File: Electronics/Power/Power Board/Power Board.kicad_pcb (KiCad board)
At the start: 2 copper layers, 70 parts, among them IC1 STM32U575VGT6, IC2 TJA1057GT/3, IC3 INA219AIDR, IC4 INA219AIDR, IC6 TPS54295PWPR, IC7 MP28167GQ-A-Z, J1 XT60PW-M, J2 USB4056-03-A, J3 XT60PW-F, J4 Screw_Terminal_01x02, J5 TC2030

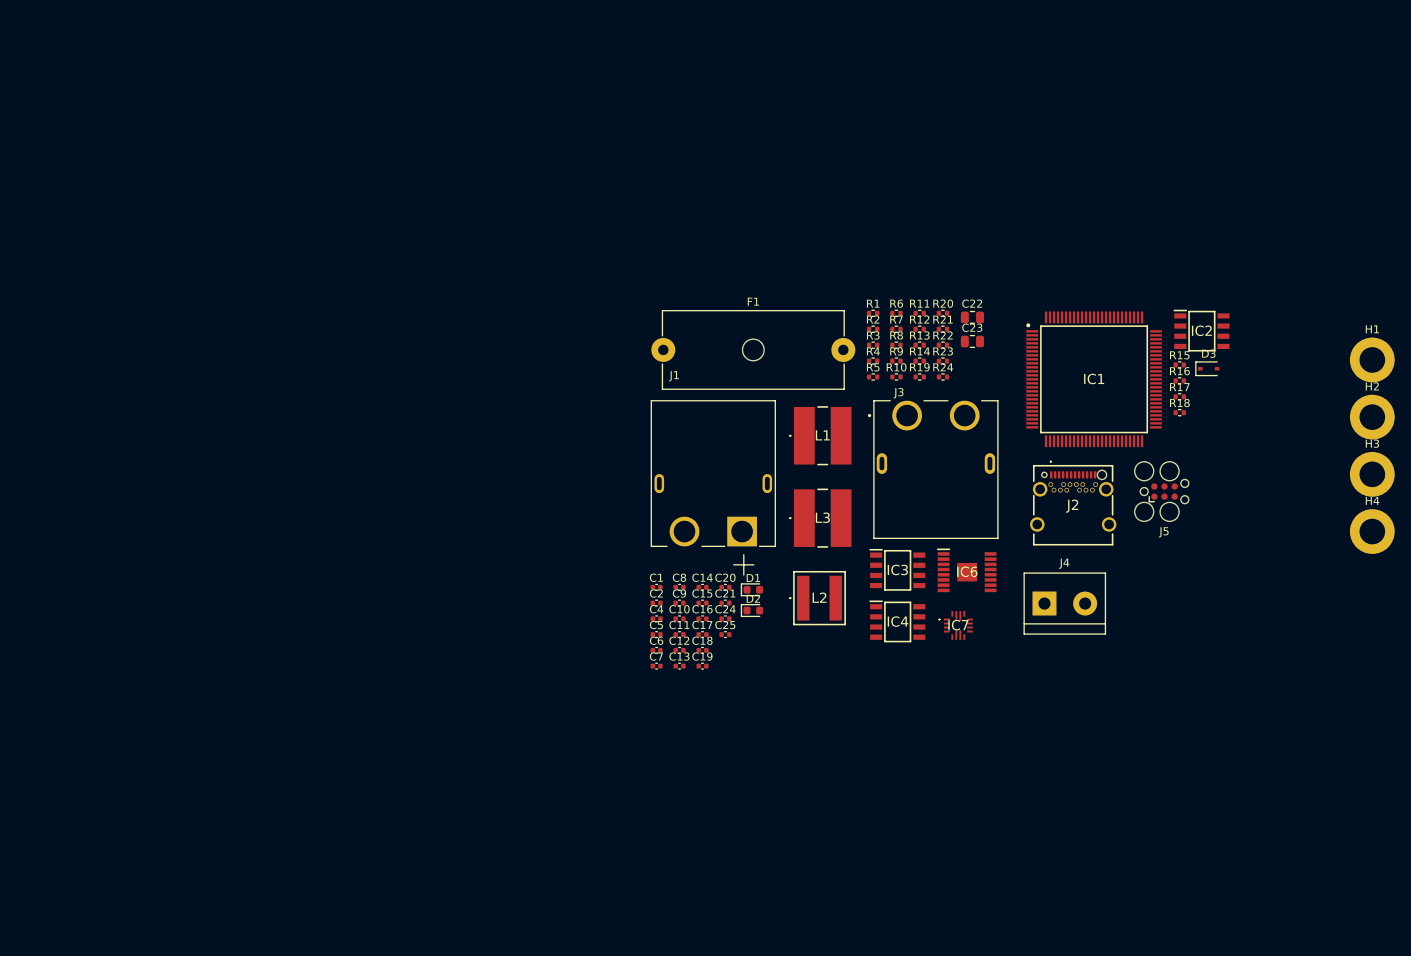
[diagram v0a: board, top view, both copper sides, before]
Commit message: Motor driver + power board progress
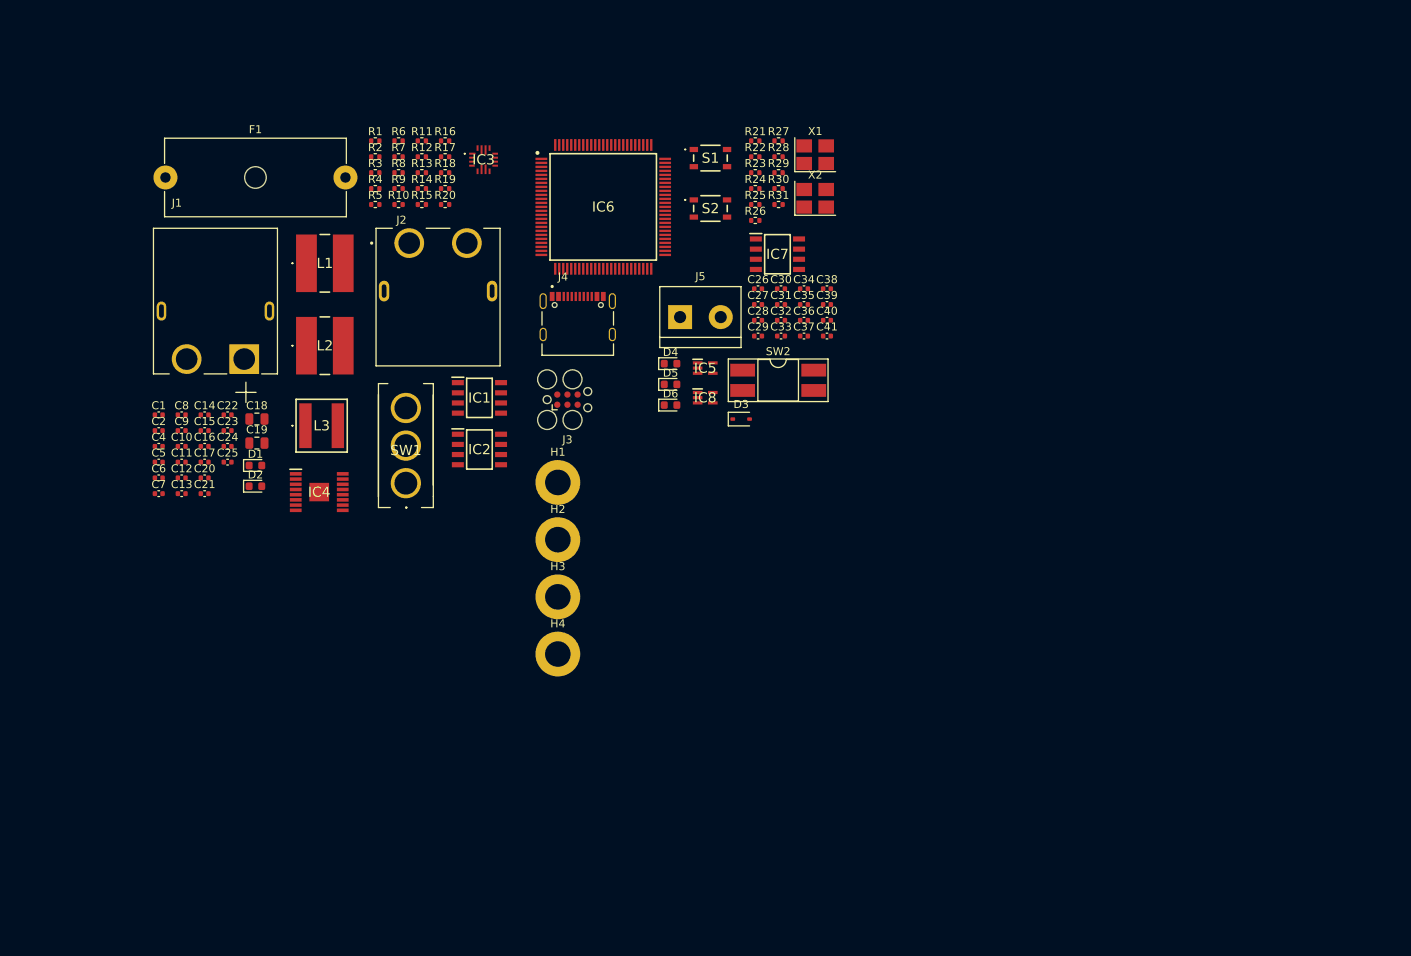
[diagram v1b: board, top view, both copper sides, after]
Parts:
- added C26: 10n, Capacitor_SMD:C_0402_1005Metric, F.Cu at (195.0, 72.2)
- added C27: 100n, Capacitor_SMD:C_0402_1005Metric, F.Cu at (195.0, 74.1)
- added C28: 100n, Capacitor_SMD:C_0402_1005Metric, F.Cu at (195.0, 76.1)
- added C29: 100n, Capacitor_SMD:C_0402_1005Metric, F.Cu at (195.0, 78.1)
- added C30: 100n, Capacitor_SMD:C_0402_1005Metric, F.Cu at (197.9, 72.2)
- added C31: 100n, Capacitor_SMD:C_0402_1005Metric, F.Cu at (197.9, 74.1)
- added C32: 100n, Capacitor_SMD:C_0402_1005Metric, F.Cu at (197.9, 76.1)
- added C33: 100n, Capacitor_SMD:C_0402_1005Metric, F.Cu at (197.9, 78.1)
- added C34: 100n, Capacitor_SMD:C_0402_1005Metric, F.Cu at (200.8, 72.2)
- added C35: 10u, Capacitor_SMD:C_0402_1005Metric, F.Cu at (200.8, 74.1)
- added C36: 4u7, Capacitor_SMD:C_0402_1005Metric, F.Cu at (200.8, 76.1)
- added C37: 100n, Capacitor_SMD:C_0402_1005Metric, F.Cu at (200.8, 78.1)
- added C38: 1u, Capacitor_SMD:C_0402_1005Metric, F.Cu at (203.6, 72.2)
- added C39: 100n, Capacitor_SMD:C_0402_1005Metric, F.Cu at (203.6, 74.1)
- added C40: 1u, Capacitor_SMD:C_0402_1005Metric, F.Cu at (203.6, 76.1)
- added C41: 10n, Capacitor_SMD:C_0402_1005Metric, F.Cu at (203.6, 78.1)
- added D4: Red, LED_SMD:LED_0603_1608Metric, F.Cu at (184.1, 81.5)
- added D5: Green, LED_SMD:LED_0603_1608Metric, F.Cu at (184.1, 84.1)
- added D6: Blue, LED_SMD:LED_0603_1608Metric, F.Cu at (184.1, 86.7)
- added IC5: ESDA6V1W5, footprints:SOT65P210X110-5N, F.Cu at (188.4, 82.1)
- added IC8: ESDA6V1W5, footprints:SOT65P210X110-5N, F.Cu at (188.4, 85.8)
- added R25: 5k1, Resistor_SMD:R_0402_1005Metric, F.Cu at (194.7, 61.6)
- added R26: 2k2, Resistor_SMD:R_0402_1005Metric, F.Cu at (194.7, 63.6)
- added R27: 10k, Resistor_SMD:R_0402_1005Metric, F.Cu at (197.6, 53.7)
- added R28: 10k, Resistor_SMD:R_0402_1005Metric, F.Cu at (197.6, 55.7)
- added R29: 1k5, Resistor_SMD:R_0402_1005Metric, F.Cu at (197.6, 57.6)
- added R30: 1k5, Resistor_SMD:R_0402_1005Metric, F.Cu at (197.6, 59.6)
- added R31: 1k5, Resistor_SMD:R_0402_1005Metric, F.Cu at (197.6, 61.6)
- added S1: TS20-42-25-WT-160-SMT-TR, MSL Footprints:TS204225WT160SMTTRMSL, F.Cu at (189.1, 55.8)
- added S2: TS20-42-25-WT-160-SMT-TR, MSL Footprints:TS204225WT160SMTTRMSL, F.Cu at (189.1, 62.1)
- added SW1: SW_SPDT, MSL Footprints:Toggle_switch, F.Cu at (151.0, 96.5)
- added SW2: SW_DIP_x02, Package_DIP:DIP-4_W8.89mm_SMDSocket_LongPads, F.Cu at (197.5, 83.6)
- added X1: 25MHz_Clock, Oscillator:Oscillator_SMD_Abracon_ASE-4Pin_3.2x2.5mm_HandSoldering, F.Cu at (202.2, 55.4)
- added X2: 32.768kHz_Clock, Oscillator:Oscillator_SMD_Abracon_ASE-4Pin_3.2x2.5mm_HandSoldering, F.Cu at (202.2, 60.8)
- C1, C17: value 10n -> 100n
- C10, C12: value 22u -> 10n
- C11: value 22u -> 1u
- C13, C14: value 22u -> 100n
- C15: value 10u -> 1u
- C16: value 10u -> 100n
- C18: value 10n -> 47u; footprint Capacitor_SMD:C_0402_1005Metric -> Capacitor_SMD:C_0805_2012Metric
- C19: value 100n -> 47u; footprint Capacitor_SMD:C_0402_1005Metric -> Capacitor_SMD:C_0805_2012Metric
- C2: value 1u -> 100n
- C21: value 1u -> 22u
- C22, C23: value 47u -> 22u; footprint Capacitor_SMD:C_0805_2012Metric -> Capacitor_SMD:C_0402_1005Metric
- C24, C25: value 100n -> 22u
- C6, C7: value 100n -> 10u
- C9: value 100n -> 10n
- IC1: value STM32U575VGT6 -> INA219AIDR; footprint MSL Footprints:QFP50P1600X1600X160-100N -> MSL Footprints:SOIC127P600X175-8N
- IC2: value TJA1057GT/3 -> INA219AIDR
- IC3: value INA219AIDR -> MP28167GQ-A-Z; footprint MSL Footprints:SOIC127P600X175-8N -> MSL Footprints:MP28167GQAZ
- IC4: value INA219AIDR -> TPS54295PWPR; footprint MSL Footprints:SOIC127P600X175-8N -> MSL Footprints:SOP65P640X120-17N
- IC6: value TPS54295PWPR -> STM32U575VGT6; footprint MSL Footprints:SOP65P640X120-17N -> MSL Footprints:QFP50P1600X1600X160-100N
- IC7: value MP28167GQ-A-Z -> TJA1057GT/3; footprint MSL Footprints:MP28167GQAZ -> MSL Footprints:SOIC127P600X175-8N
- J2: value USB4056-03-A -> XT60PW-F; footprint MSL Footprints:USB405603A -> MSL Footprints:AMASS_XT60PW-F
- J3: value XT60PW-F -> TC2030; footprint MSL Footprints:AMASS_XT60PW-F -> Connector:Tag-Connect_TC2030-IDC-FP_2x03_P1.27mm_Vertical
- J4: value Screw_Terminal_01x02 -> TYPE-C-31-M-12; footprint TerminalBlock:TerminalBlock_bornier-2_P5.08mm -> MSL Footprints:HRO_TYPE-C-31-M-12
- J5: value TC2030 -> Screw_Terminal_01x02; footprint Connector:Tag-Connect_TC2030-IDC-FP_2x03_P1.27mm_Vertical -> TerminalBlock:TerminalBlock_bornier-2_P5.08mm
- L2: value MPL-AL6050-4R7 -> 2u2; footprint MSL Footprints:MPLAL60504R7 -> MSL Footprints:29222C
- L3: value 2u2 -> MPL-AL6050-4R7; footprint MSL Footprints:29222C -> MSL Footprints:MPLAL60504R7
- R1: value 100k -> 22R
- R10: value 22k1 -> 787k
- R11: value 33k -> 0R
- R12: value 10k -> 0R
- R13: value 2k2 -> 430k
- R14: value 1k5 -> 39k2
- R15: value 5k1 -> 124k
- R16: value 5k1 -> 22k1
- R17: value 2k2 -> 33k
- R18: value 2k2 -> 10k
- R19, R23: value 10m -> 2k2
- R2: value 10k -> 10m
- R20: value 22R -> 1k5
- R21: value 22R -> 120R
- R22: value 22R -> 10k
- R24: value 22R -> 5k1
- R3, R4: value 0R -> 22R
- R5: value 430k -> 10m
- R6: value 787k -> 22R
- R7: value 39k2 -> 10k
- R8: value 21k5 -> 100k
- R9: value 124k -> 21k5
- moved H1 103.0 mm to (170.0, 96.4)
- moved H2 103.0 mm to (170.0, 103.5)
- moved H3 103.0 mm to (170.0, 110.7)
- moved H4 103.0 mm to (170.0, 117.8)
- moved R15 96.8 mm to (153.0, 61.6)
- moved R16 96.6 mm to (155.9, 53.7)
- moved R17 96.6 mm to (155.9, 55.7)
- moved R18 96.6 mm to (155.9, 57.6)
- moved C22 93.9 mm to (128.7, 87.9)
- moved C23 93.8 mm to (128.7, 89.9)
- moved IC2 91.5 mm to (160.2, 92.2)
- moved J2 85.9 mm to (155.0, 66.4)
- moved IC1 76.9 mm to (160.2, 85.8)
- moved IC4 74.1 mm to (140.2, 97.6)
- moved IC3 72.9 mm to (160.7, 56.0)
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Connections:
- C1 pad 1: GND -> /Power/12V_VIN+
- C1 pad 2: /Power/12V_EN -> /Power/12V_VIN-
- C10 pad 1: +12V -> GND
- C10 pad 2: GND -> /Power/12V_EN
- C11 pad 1: +12V -> GND
- C11 pad 2: GND -> /Power/3V65
- C12 pad 1: +12V -> /Power/OC
- C13 pad 1: +12V -> /Power/VBST1
- C13 pad 2: GND -> /Power/SW1
- C14 pad 1: +12V -> /Power/VBST2
- C14 pad 2: GND -> /Power/SW2
- C15 pad 1: VBAT -> /Power/VREG5
- C16 pad 1: VBAT -> /Power/12V_SW1
- C16 pad 2: GND -> /Power/BST12
- C17 pad 1: GND -> /Power/BST22
- C17 pad 2: /Power/SS1 -> /Power/12V_SW2
- C18 pad 1: GND -> +5V
- C18 pad 2: /Power/SS2 -> GND
- C19 pad 1: /Power/VBST1 -> +3V3
- C19 pad 2: /Power/SW1 -> GND
- C2 pad 1: GND -> /Power/BAT_VIN+
- C2 pad 2: /Power/3V65 -> /Power/BAT_VIN-
- C20 pad 1: /Power/VBST2 -> +12V
- C20 pad 2: /Power/SW2 -> GND
- C21 pad 1: /Power/VREG5 -> +12V
- C22 pad 1: +5V -> +12V
- C23 pad 1: +3V3 -> +12V
- C24 pad 1: /Power/12V_VIN+ -> +12V
- C24 pad 2: /Power/12V_VIN- -> GND
- C25 pad 1: /Power/BAT_VIN+ -> +12V
- C25 pad 2: /Power/BAT_VIN- -> GND
- C6 pad 1: /Power/12V_SW1 -> VBAT
- C6 pad 2: /Power/BST12 -> GND
- C7 pad 1: /Power/BST22 -> VBAT
- C7 pad 2: /Power/12V_SW2 -> GND
- C8 pad 1: /Power/OC -> GND
- C8 pad 2: GND -> /Power/SS1
- C9 pad 1: +12V -> GND
- C9 pad 2: GND -> /Power/SS2
- IC1 pad 1: unconnected-(IC1-PE2-Pad1) -> GND
- IC1 pad 2: unconnected-(IC1-PE3-Pad2) -> GND
- IC1 pad 3: unconnected-(IC1-PE4-Pad3) -> SDA
- IC1 pad 4: unconnected-(IC1-PE5-Pad4) -> SCL
- IC1 pad 5: unconnected-(IC1-PE6-Pad5) -> +3V3
- IC1 pad 6: unconnected-(IC1-VBAT-Pad6) -> GND
- IC1 pad 7: unconnected-(IC1-PC13-Pad7) -> /Power/12V_VIN-
- IC1 pad 8: OSC32_IN -> /Power/12V_VIN+
- IC2 pad 1: CAN_TX -> GND
- IC2 pad 2: GND -> +3V3
- IC2 pad 3: +5V -> SDA
- IC2 pad 4: CAN_RX -> SCL
- IC2 pad 6: /Control/CANL -> GND
- IC2 pad 7: /Control/CANH -> /Power/BAT_VIN-
- IC2 pad 8: SILENT -> /Power/BAT_VIN+
- IC3 pad 1: GND -> VBAT
- IC3 pad 3: SDA -> /Power/12V_EN
- IC3 pad 4: SCL -> ALT
- IC3 pad 5: +3V3 -> SCL
- IC3 pad 6: GND -> SDA
- IC3 pad 7: /Power/12V_VIN- -> /Power/OC
- IC3 pad 8: /Power/12V_VIN+ -> /Power/12V_FB
- IC4 pad 1: GND -> VBAT
- IC4 pad 2: +3V3 -> /Power/VBST1
- IC4 pad 3: SDA -> /Power/SW1
- IC4 pad 4: SCL -> GND
- IC4 pad 5: +3V3 -> VBAT
- IC4 pad 6: GND -> /Power/SS1
- IC4 pad 7: /Power/BAT_VIN- -> /Power/VFB1
- IC4 pad 8: /Power/BAT_VIN+ -> GND
- IC6 pad 1: VBAT -> unconnected-(IC6-PE2-Pad1)
- IC6 pad 10: /Power/VFB2 -> GND
- IC6 pad 11: /Power/SS2 -> +3V3
- IC6 pad 12: VBAT -> OSC25M
- IC6 pad 13: GND -> unconnected-(IC6-PH1-OSC_OUT-Pad13)
- IC6 pad 14: /Power/SW2 -> NRST
- IC6 pad 15: /Power/VBST2 -> unconnected-(IC6-PC0-Pad15)
- IC6 pad 16: VBAT -> unconnected-(IC6-PC1-Pad16)
- IC6 pad 17: GND -> unconnected-(IC6-PC2-Pad17)
- IC6 pad 2: /Power/VBST1 -> unconnected-(IC6-PE3-Pad2)
- IC6 pad 3: /Power/SW1 -> unconnected-(IC6-PE4-Pad3)
- IC6 pad 4: GND -> unconnected-(IC6-PE5-Pad4)
- IC6 pad 5: VBAT -> unconnected-(IC6-PE6-Pad5)
- IC6 pad 6: /Power/SS1 -> +3V3
- IC6 pad 7: /Power/VFB1 -> unconnected-(IC6-PC13-Pad7)
- IC6 pad 8: GND -> OSC32K
- IC6 pad 9: /Power/VREG5 -> unconnected-(IC6-PC15-OSC32_OUT-Pad9)
- IC7 pad 1: VBAT -> CAN_TX
- IC7 pad 3: /Power/12V_EN -> +5V
- IC7 pad 4: ALT -> CAN_RX
- IC7 pad 5: SCL -> +3V3
- IC7 pad 6: SDA -> /Control/CANL
- IC7 pad 7: /Power/OC -> /Control/CANH
- IC7 pad 8: /Power/12V_FB -> SILENT
- J3 pad 1: GND -> +3V3
- J3 pad 2: /Power/12V_OUT -> SWDIO
- J5 pad 1: +3V3 -> /Control/CANH
- J5 pad 2: SWDIO -> /Control/CANL
- L2 pad 1: /Power/12V_SW1 -> /Power/SW2
- L2 pad 2: /Power/12V_SW2 -> +3V3
- L3 pad 1: /Power/SW2 -> /Power/12V_SW1
- L3 pad 2: +3V3 -> /Power/12V_SW2
- R1 pad 1: VBAT -> +12V
- R1 pad 2: /Power/12V_EN -> /Power/12V_VIN+
- R10 pad 1: /Power/VFB1 -> /Power/12V_FB
- R10 pad 2: GND -> /Power/12V_FB_MID
- R11 pad 1: +3V3 -> /Power/BST11
- R11 pad 2: /Power/VFB2 -> /Power/BST12
- R12 pad 1: /Power/VFB2 -> /Power/BST22
- R12 pad 2: GND -> /Power/BST21
- R13 pad 1: /Power/LED_5V -> +12V
- R13 pad 2: GND -> /Power/12V_FB_MID
- R14 pad 1: /Power/LED_3V3 -> /Power/12V_FB_MID
- R15 pad 1: /Control/CC2 -> +5V
- R15 pad 2: GND -> /Power/VFB1
- R16 pad 1: /Control/CC1 -> /Power/VFB1
- R17 pad 2: SCL -> /Power/VFB2
- R18 pad 1: +3V3 -> /Power/VFB2
- R18 pad 2: SDA -> GND
- R19 pad 1: /Power/12V_OUT -> /Power/LED_5V
- R19 pad 2: +12V -> GND
- R2 pad 1: +3.3V -> /Power/12V_OUT
- R2 pad 2: ALT -> +12V
- R20 pad 1: /Power/12V_OUT -> /Power/LED_3V3
- R20 pad 2: /Power/12V_VIN- -> GND
- R21 pad 1: +12V -> /Control/CANL
- R21 pad 2: /Power/12V_VIN+ -> /Control/CAN_SW
- R22 pad 1: /Power/VBAT_SWITCHED -> BOOT0
- R22 pad 2: /Power/BAT_VIN+ -> GND
- R23 pad 1: VBAT -> +3V3
- R23 pad 2: /Power/VBAT_SWITCHED -> SCL
- R24 pad 1: VBAT -> /Control/CC1
- R24 pad 2: /Power/BAT_VIN- -> GND
- R3 pad 1: /Power/BST11 -> /Power/12V_OUT
- R3 pad 2: /Power/BST12 -> /Power/12V_VIN-
- R4 pad 1: /Power/BST22 -> /Power/VBAT_SWITCHED
- R4 pad 2: /Power/BST21 -> /Power/BAT_VIN+
- R5 pad 1: +12V -> VBAT
- R5 pad 2: /Power/12V_FB_MID -> /Power/VBAT_SWITCHED
- R6 pad 1: /Power/12V_FB -> VBAT
- R6 pad 2: /Power/12V_FB_MID -> /Power/BAT_VIN-
- R7 pad 1: /Power/12V_FB_MID -> +3.3V
- R7 pad 2: GND -> ALT
- R8 pad 1: /Power/OC -> VBAT
- R8 pad 2: GND -> /Power/12V_EN
- R9 pad 1: +5V -> /Power/OC
- R9 pad 2: /Power/VFB1 -> GND

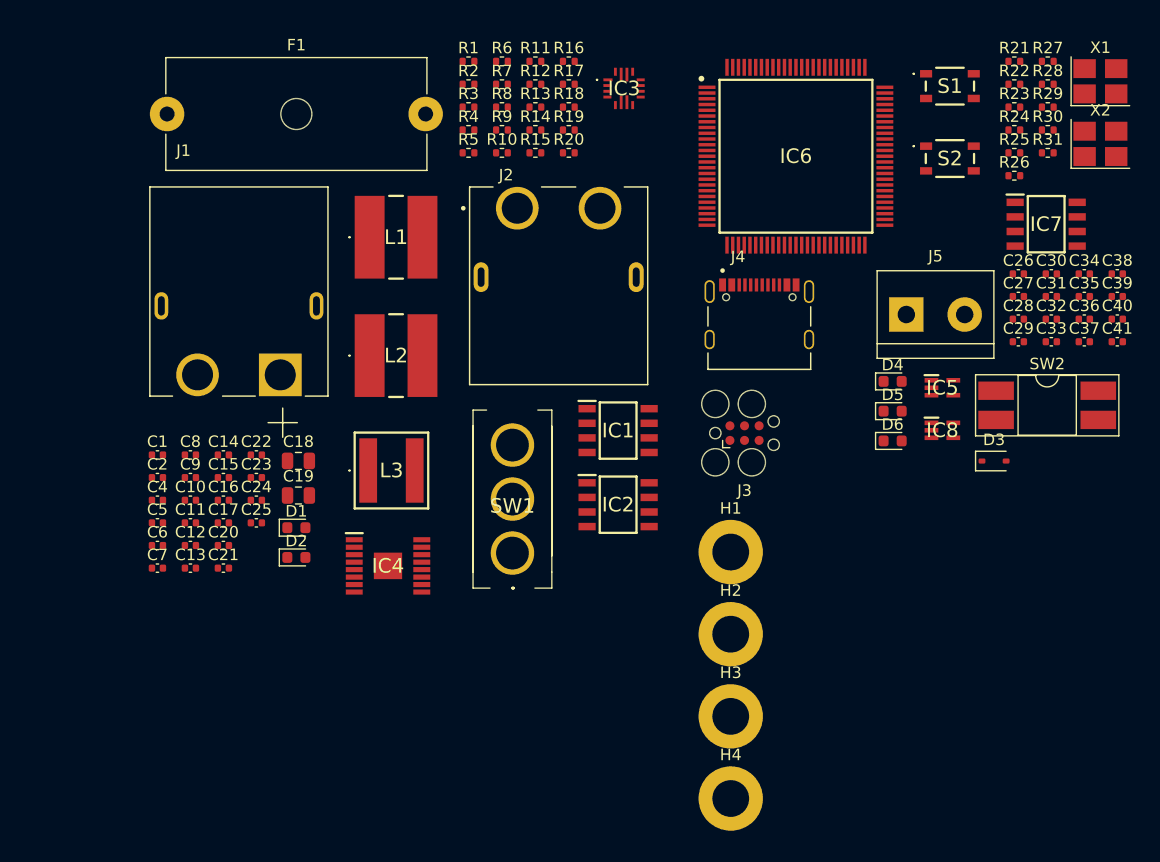
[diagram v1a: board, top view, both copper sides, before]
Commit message: Schematic updates
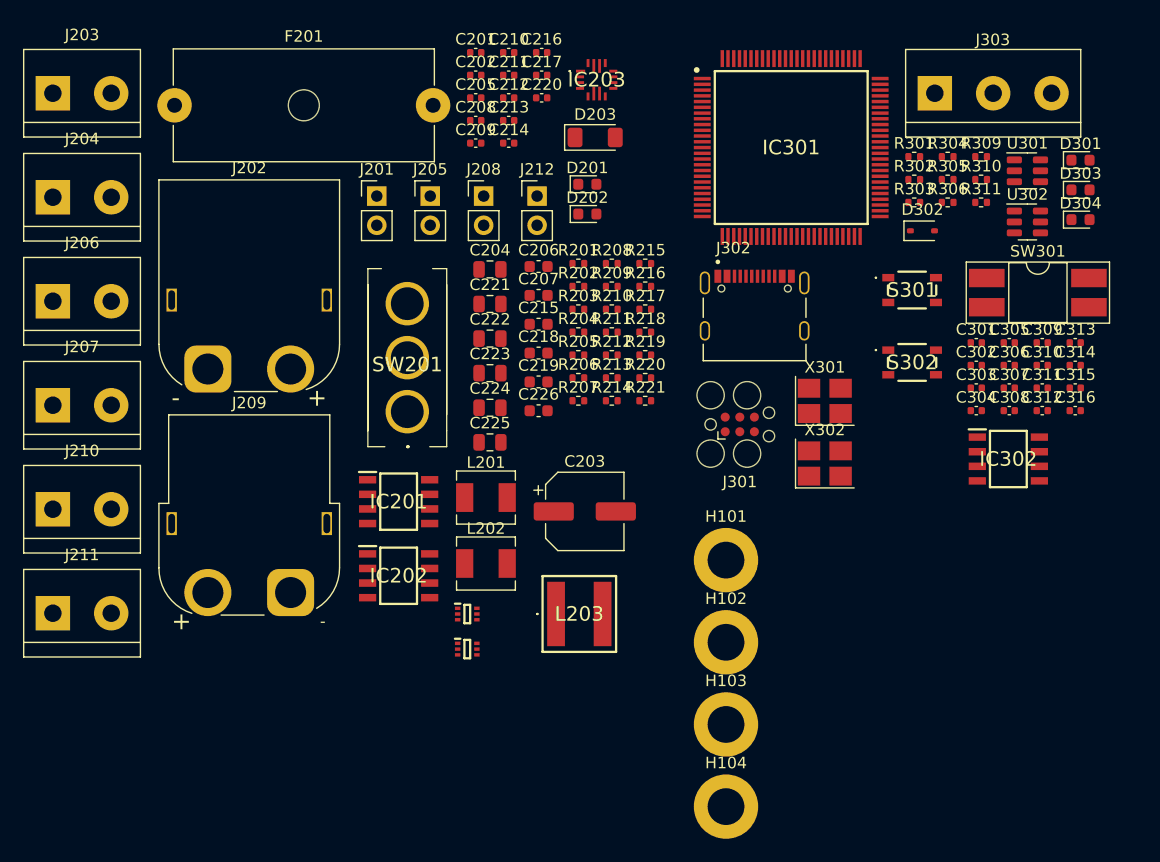
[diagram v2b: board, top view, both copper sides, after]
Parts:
- removed C1, C13, C14, C16, C17, C2, C20, C27, C28, C29, C30, C31, C32, C33, C34, C37, C39, C5: 100n, Capacitor_SMD:C_0402_1005Metric
- removed C10, C12, C26, C41, C8, C9: 10n, Capacitor_SMD:C_0402_1005Metric
- removed C11, C15, C38, C40: 1u, Capacitor_SMD:C_0402_1005Metric
- removed C18, C19: 47u, Capacitor_SMD:C_0805_2012Metric
- removed C21, C22, C23, C24, C25, C4: 22u, Capacitor_SMD:C_0402_1005Metric
- removed C35, C6, C7: 10u, Capacitor_SMD:C_0402_1005Metric
- removed C36: 4u7, Capacitor_SMD:C_0402_1005Metric
- removed D1, D2: LED_R, LED_SMD:LED_0603_1608Metric
- removed D3: BAT760-115, Diode_SMD:D_SOD-323
- removed D4: Red, LED_SMD:LED_0603_1608Metric
- removed D5: Green, LED_SMD:LED_0603_1608Metric
- removed D6: Blue, LED_SMD:LED_0603_1608Metric
- removed F1: 10A, Fuse:Fuseholder_Cylinder-5x20mm_Schurter_0031_8201_Horizontal_Open
- removed H1, H2, H3, H4: MountingHole_Pad, MountingHole:MountingHole_3.2mm_M3_DIN965_Pad
- removed IC1, IC2: INA219AIDR, MSL Footprints:SOIC127P600X175-8N
- removed IC3: MP28167GQ-A-Z, MSL Footprints:MP28167GQAZ
- removed IC4: TPS54295PWPR, MSL Footprints:SOP65P640X120-17N
- removed IC5, IC8: ESDA6V1W5, footprints:SOT65P210X110-5N
- removed IC6: STM32U575VGT6, MSL Footprints:QFP50P1600X1600X160-100N
- removed IC7: TJA1057GT/3, MSL Footprints:SOIC127P600X175-8N
- removed J1: XT60PW-M, MSL Footprints:AMASS_XT60PW-M
- removed J2: XT60PW-F, MSL Footprints:AMASS_XT60PW-F
- removed J3: TC2030, Connector:Tag-Connect_TC2030-IDC-FP_2x03_P1.27mm_Vertical
- removed J4: TYPE-C-31-M-12, MSL Footprints:HRO_TYPE-C-31-M-12
- removed J5: Screw_Terminal_01x02, TerminalBlock:TerminalBlock_bornier-2_P5.08mm
- removed L1: 3u3, MSL Footprints:29332C
- removed L2: 2u2, MSL Footprints:29222C
- removed L3: MPL-AL6050-4R7, MSL Footprints:MPLAL60504R7
- removed R1, R3, R4, R6: 22R, Resistor_SMD:R_0402_1005Metric
- removed R10: 787k, Resistor_SMD:R_0402_1005Metric
- removed R11, R12: 0R, Resistor_SMD:R_0402_1005Metric
- removed R13: 430k, Resistor_SMD:R_0402_1005Metric
- removed R14: 39k2, Resistor_SMD:R_0402_1005Metric
- removed R15: 124k, Resistor_SMD:R_0402_1005Metric
- removed R16: 22k1, Resistor_SMD:R_0402_1005Metric
- removed R17: 33k, Resistor_SMD:R_0402_1005Metric
- removed R18, R22, R27, R28, R7: 10k, Resistor_SMD:R_0402_1005Metric
- removed R19, R23, R26: 2k2, Resistor_SMD:R_0402_1005Metric
- removed R2, R5: 10m, Resistor_SMD:R_0402_1005Metric
- removed R20, R29, R30, R31: 1k5, Resistor_SMD:R_0402_1005Metric
- removed R21: 120R, Resistor_SMD:R_0402_1005Metric
- removed R24, R25: 5k1, Resistor_SMD:R_0402_1005Metric
- removed R8: 100k, Resistor_SMD:R_0402_1005Metric
- removed R9: 21k5, Resistor_SMD:R_0402_1005Metric
- removed S1, S2: TS20-42-25-WT-160-SMT-TR, MSL Footprints:TS204225WT160SMTTRMSL
- removed SW1: SW_SPDT, MSL Footprints:Toggle_switch
- removed SW2: SW_DIP_x02, Package_DIP:DIP-4_W8.89mm_SMDSocket_LongPads
- removed X1: 25MHz_Clock, Oscillator:Oscillator_SMD_Abracon_ASE-4Pin_3.2x2.5mm_HandSoldering
- removed X2: 32.768kHz_Clock, Oscillator:Oscillator_SMD_Abracon_ASE-4Pin_3.2x2.5mm_HandSoldering
- added C201: 100n, Capacitor_SMD:C_0402_1005Metric, F.Cu at (147.8, 52.9)
- added C202: 100n, Capacitor_SMD:C_0402_1005Metric, F.Cu at (147.8, 54.9)
- added C203: 100u, Capacitor_SMD:CP_Elec_6.3x7.7, F.Cu at (157.3, 92.8)
- added C204: 22u, Capacitor_SMD:C_0805_2012Metric, F.Cu at (149.0, 71.8)
- added C205: 100n, Capacitor_SMD:C_0402_1005Metric, F.Cu at (147.8, 56.8)
- added C206: 22u, Capacitor_SMD:C_0603_1608Metric, F.Cu at (153.3, 71.5)
- added C207: 22u, Capacitor_SMD:C_0603_1608Metric, F.Cu at (153.3, 74.0)
- added C208: 100n, Capacitor_SMD:C_0402_1005Metric, F.Cu at (147.8, 58.8)
- added C209: 100n, Capacitor_SMD:C_0402_1005Metric, F.Cu at (147.8, 60.8)
- added C210: 10n, Capacitor_SMD:C_0402_1005Metric, F.Cu at (150.7, 52.9)
- added C211: 1u, Capacitor_SMD:C_0402_1005Metric, F.Cu at (150.7, 54.9)
- added C212: 10n, Capacitor_SMD:C_0402_1005Metric, F.Cu at (150.7, 56.8)
- added C213: 100n, Capacitor_SMD:C_0402_1005Metric, F.Cu at (150.7, 58.8)
- added C214: 100n, Capacitor_SMD:C_0402_1005Metric, F.Cu at (150.7, 60.8)
- added C215: 22u, Capacitor_SMD:C_0603_1608Metric, F.Cu at (153.3, 76.5)
- added C216: 100n, Capacitor_SMD:C_0402_1005Metric, F.Cu at (153.5, 52.9)
- added C217: 100n, Capacitor_SMD:C_0402_1005Metric, F.Cu at (153.5, 54.9)
- added C218: 22u, Capacitor_SMD:C_0603_1608Metric, F.Cu at (153.3, 79.0)
- added C219: 22u, Capacitor_SMD:C_0603_1608Metric, F.Cu at (153.3, 81.6)
- added C220: 100n, Capacitor_SMD:C_0402_1005Metric, F.Cu at (153.5, 56.8)
- added C221: 22u, Capacitor_SMD:C_0805_2012Metric, F.Cu at (149.0, 74.8)
- added C222: 22u, Capacitor_SMD:C_0805_2012Metric, F.Cu at (149.0, 77.8)
- added C223: 22u, Capacitor_SMD:C_0805_2012Metric, F.Cu at (149.0, 80.8)
- added C224: 22u, Capacitor_SMD:C_0805_2012Metric, F.Cu at (149.0, 83.8)
- added C225: 22u, Capacitor_SMD:C_0805_2012Metric, F.Cu at (149.0, 86.8)
- added C226: 22u, Capacitor_SMD:C_0603_1608Metric, F.Cu at (153.3, 84.1)
- added C301: 100n, Capacitor_SMD:C_0402_1005Metric, F.Cu at (191.4, 78.1)
- added C302: 100n, Capacitor_SMD:C_0402_1005Metric, F.Cu at (191.4, 80.1)
- added C303: 10n, Capacitor_SMD:C_0402_1005Metric, F.Cu at (191.4, 82.1)
- added C304: 10n, Capacitor_SMD:C_0402_1005Metric, F.Cu at (191.4, 84.1)
- added C305: 100n, Capacitor_SMD:C_0402_1005Metric, F.Cu at (194.2, 78.1)
- added C306: 1u, Capacitor_SMD:C_0402_1005Metric, F.Cu at (194.2, 80.1)
- added C307: 100n, Capacitor_SMD:C_0402_1005Metric, F.Cu at (194.2, 82.1)
- added C308: 1u, Capacitor_SMD:C_0402_1005Metric, F.Cu at (194.2, 84.1)
- added C309: 4u7, Capacitor_SMD:C_0402_1005Metric, F.Cu at (197.1, 78.1)
- added C310: 100n, Capacitor_SMD:C_0402_1005Metric, F.Cu at (197.1, 80.1)
- added C311: 100n, Capacitor_SMD:C_0402_1005Metric, F.Cu at (197.1, 82.1)
- added C312: 100n, Capacitor_SMD:C_0402_1005Metric, F.Cu at (197.1, 84.1)
- added C313: 100n, Capacitor_SMD:C_0402_1005Metric, F.Cu at (200.0, 78.1)
- added C314: 100n, Capacitor_SMD:C_0402_1005Metric, F.Cu at (200.0, 80.1)
- added C315: 100n, Capacitor_SMD:C_0402_1005Metric, F.Cu at (200.0, 82.1)
- added C316: 10u, Capacitor_SMD:C_0402_1005Metric, F.Cu at (200.0, 84.1)
- added D201: GREEN, LED_SMD:LED_0603_1608Metric, F.Cu at (157.5, 64.4)
- added D202: GREEN, LED_SMD:LED_0603_1608Metric, F.Cu at (157.5, 66.9)
- added D203: ZMM10V, Diode_SMD:D_MiniMELF, F.Cu at (158.2, 60.3)
- added D301: Red, LED_SMD:LED_0603_1608Metric, F.Cu at (200.4, 62.3)
- added D302: BAT760-115, Diode_SMD:D_SOD-323, F.Cu at (186.7, 68.4)
- added D303: Green, LED_SMD:LED_0603_1608Metric, F.Cu at (200.4, 64.8)
- added D304: Blue, LED_SMD:LED_0603_1608Metric, F.Cu at (200.4, 67.4)
- added F201: 10A, Fuse:Fuseholder_Cylinder-5x20mm_Schurter_0031_8201_Horizontal_Open, F.Cu at (121.6, 57.5)
- added H101: MountingHole_Pad, MountingHole:MountingHole_3.2mm_M3_DIN965_Pad, F.Cu at (169.6, 97.1)
- added H102: MountingHole_Pad, MountingHole:MountingHole_3.2mm_M3_DIN965_Pad, F.Cu at (169.6, 104.2)
- added H103: MountingHole_Pad, MountingHole:MountingHole_3.2mm_M3_DIN965_Pad, F.Cu at (169.6, 111.4)
- added H104: MountingHole_Pad, MountingHole:MountingHole_3.2mm_M3_DIN965_Pad, F.Cu at (169.6, 118.5)
- added IC201: INA219AIDR, MSL Footprints:SOIC127P600X175-8N, F.Cu at (141.1, 92.0)
- added IC202: INA219AIDR, MSL Footprints:SOIC127P600X175-8N, F.Cu at (141.1, 98.4)
- added IC203: MP28167GQ-A-Z, MSL Footprints:MP28167GQAZ, F.Cu at (158.3, 55.3)
- added IC204: TPS563202DRLR, MSL Footprints:SOTFL50P160X60-6N, F.Cu at (147.1, 101.8)
- added IC206: TPS563202DRLR, MSL Footprints:SOTFL50P160X60-6N, F.Cu at (147.1, 104.8)
- added IC301: STM32U575VGT6, MSL Footprints:QFP50P1600X1600X160-100N, F.Cu at (175.3, 61.2)
- added IC302: TJA1057GT/3, MSL Footprints:SOIC127P600X175-8N, F.Cu at (194.2, 88.3)
- added J201: Conn_01x02_Pin, Connector_PinHeader_2.54mm:PinHeader_1x02_P2.54mm_Vertical, F.Cu at (139.2, 65.4)
- added J202: XT60PW-M, Connector_AMASS:AMASS_XT60PW-M_1x02_P7.20mm_Horizontal, F.Cu at (124.5, 80.4)
- added J203: Screw_Terminal_01x02, TerminalBlock:TerminalBlock_bornier-2_P5.08mm, F.Cu at (111.0, 56.4)
- added J204: Screw_Terminal_01x02, TerminalBlock:TerminalBlock_bornier-2_P5.08mm, F.Cu at (111.0, 65.5)
- added J205: Conn_01x02_Pin, Connector_PinHeader_2.54mm:PinHeader_1x02_P2.54mm_Vertical, F.Cu at (143.8, 65.4)
- added J206: Screw_Terminal_01x02, TerminalBlock:TerminalBlock_bornier-2_P5.08mm, F.Cu at (111.0, 74.5)
- added J207: Screw_Terminal_01x02, TerminalBlock:TerminalBlock_bornier-2_P5.08mm, F.Cu at (111.0, 83.6)
- added J208: Conn_01x02_Pin, Connector_PinHeader_2.54mm:PinHeader_1x02_P2.54mm_Vertical, F.Cu at (148.5, 65.4)
- added J209: XT60PW-F, Connector_AMASS:AMASS_XT60PW-F_1x02_P7.20mm_Horizontal, F.Cu at (131.7, 99.9)
- added J210: Screw_Terminal_01x02, TerminalBlock:TerminalBlock_bornier-2_P5.08mm, F.Cu at (111.0, 92.6)
- added J211: Screw_Terminal_01x02, TerminalBlock:TerminalBlock_bornier-2_P5.08mm, F.Cu at (111.0, 101.7)
- added J212: Conn_01x02_Pin, Connector_PinHeader_2.54mm:PinHeader_1x02_P2.54mm_Vertical, F.Cu at (153.1, 65.4)
- added J301: TC2030, Connector:Tag-Connect_TC2030-IDC-FP_2x03_P1.27mm_Vertical, F.Cu at (170.8, 85.3)
- added J302: TYPE-C-31-M-12, MSL Footprints:HRO_TYPE-C-31-M-12, F.Cu at (172.1, 77.1)
- added J303: Screw_Terminal_01x03, TerminalBlock:TerminalBlock_bornier-3_P5.08mm, F.Cu at (187.8, 56.4)
- added L201: 4u7, Inductor_SMD:L_Chilisin_BMRA00040420, F.Cu at (148.7, 91.6)
- added L202: 3u3, Inductor_SMD:L_Chilisin_BMRA00040420, F.Cu at (148.7, 97.4)
- added L203: MPL-AL6050-4R7, MSL Footprints:MPLAL60504R7, F.Cu at (156.8, 101.8)
- added R201: 22R, Resistor_SMD:R_0402_1005Metric, F.Cu at (156.7, 71.3)
- added R202: 10m, Resistor_SMD:R_0402_1005Metric, F.Cu at (156.7, 73.2)
- added R203: 22R, Resistor_SMD:R_0402_1005Metric, F.Cu at (156.7, 75.2)
- added R204: 22R, Resistor_SMD:R_0402_1005Metric, F.Cu at (156.7, 77.2)
- added R205: 10m, Resistor_SMD:R_0402_1005Metric, F.Cu at (156.7, 79.2)
- added R206: 22R, Resistor_SMD:R_0402_1005Metric, F.Cu at (156.7, 81.2)
- added R207: 10k, Resistor_SMD:R_0402_1005Metric, F.Cu at (156.7, 83.2)
- added R208: 100k, Resistor_SMD:R_0402_1005Metric, F.Cu at (159.6, 71.3)
- added R209: 21k5, Resistor_SMD:R_0402_1005Metric, F.Cu at (159.6, 73.2)
- added R210: 787k, Resistor_SMD:R_0402_1005Metric, F.Cu at (159.6, 75.2)
- added R211: 0R, Resistor_SMD:R_0402_1005Metric, F.Cu at (159.6, 77.2)
- added R212: 0R, Resistor_SMD:R_0402_1005Metric, F.Cu at (159.6, 79.2)
- added R213: 430k, Resistor_SMD:R_0402_1005Metric, F.Cu at (159.6, 81.2)
- added R214: 39k2, Resistor_SMD:R_0402_1005Metric, F.Cu at (159.6, 83.2)
- added R215: 52k, Resistor_SMD:R_0402_1005Metric, F.Cu at (162.6, 71.3)
- added R216: 10k, Resistor_SMD:R_0402_1005Metric, F.Cu at (162.6, 73.2)
- added R217: 31k, Resistor_SMD:R_0402_1005Metric, F.Cu at (162.6, 75.2)
- added R218: 10k, Resistor_SMD:R_0402_1005Metric, F.Cu at (162.6, 77.2)
- added R219: 2k2, Resistor_SMD:R_0402_1005Metric, F.Cu at (162.6, 79.2)
- added R220: 1k5, Resistor_SMD:R_0402_1005Metric, F.Cu at (162.6, 81.2)
- added R221: 330R, Resistor_SMD:R_0402_1005Metric, F.Cu at (162.6, 83.2)
- added R301: 120R, Resistor_SMD:R_0402_1005Metric, F.Cu at (186.0, 62.0)
- added R302: 10k, Resistor_SMD:R_0402_1005Metric, F.Cu at (186.0, 63.9)
- added R303: 10k, Resistor_SMD:R_0402_1005Metric, F.Cu at (186.0, 65.9)
- added R304: 10k, Resistor_SMD:R_0402_1005Metric, F.Cu at (188.9, 62.0)
- added R305: 2k2, Resistor_SMD:R_0402_1005Metric, F.Cu at (188.9, 63.9)
- added R306: 2k2, Resistor_SMD:R_0402_1005Metric, F.Cu at (188.9, 65.9)
- added R309: 1k5, Resistor_SMD:R_0402_1005Metric, F.Cu at (191.8, 62.0)
- added R310: 1k5, Resistor_SMD:R_0402_1005Metric, F.Cu at (191.8, 63.9)
- added R311: 1k5, Resistor_SMD:R_0402_1005Metric, F.Cu at (191.8, 65.9)
- added S301: TS20-42-25-WT-160-SMT-TR, MSL Footprints:TS204225WT160SMTTRMSL, F.Cu at (185.8, 73.6)
- added S302: TS20-42-25-WT-160-SMT-TR, MSL Footprints:TS204225WT160SMTTRMSL, F.Cu at (185.8, 79.9)
- added SW201: SW_SPDT, MSL Footprints:Toggle_switch, F.Cu at (141.8, 84.1)
- added SW301: SW_DIP_x02, Package_DIP:DIP-4_W8.89mm_SMDSocket_LongPads, F.Cu at (196.7, 73.8)
- added U301: USBLC6-4SC6-ES, Package_TO_SOT_SMD:SOT-23-6, F.Cu at (195.8, 63.2)
- added U302: USBLC6-4SC6-ES, Package_TO_SOT_SMD:SOT-23-6, F.Cu at (195.8, 67.6)
- added X301: 25MHz_Clock, Oscillator:Oscillator_SMD_Abracon_ASE-4Pin_3.2x2.5mm_HandSoldering, F.Cu at (178.2, 83.2)
- added X302: 32.768kHz_Clock, Oscillator:Oscillator_SMD_Abracon_ASE-4Pin_3.2x2.5mm_HandSoldering, F.Cu at (178.2, 88.7)
